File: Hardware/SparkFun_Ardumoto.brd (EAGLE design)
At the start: 59.7 x 53.3 mm, 33 parts, among them U1 ARDUINO, U2 L298, U3 74HC1G04, U4 74HC1G04

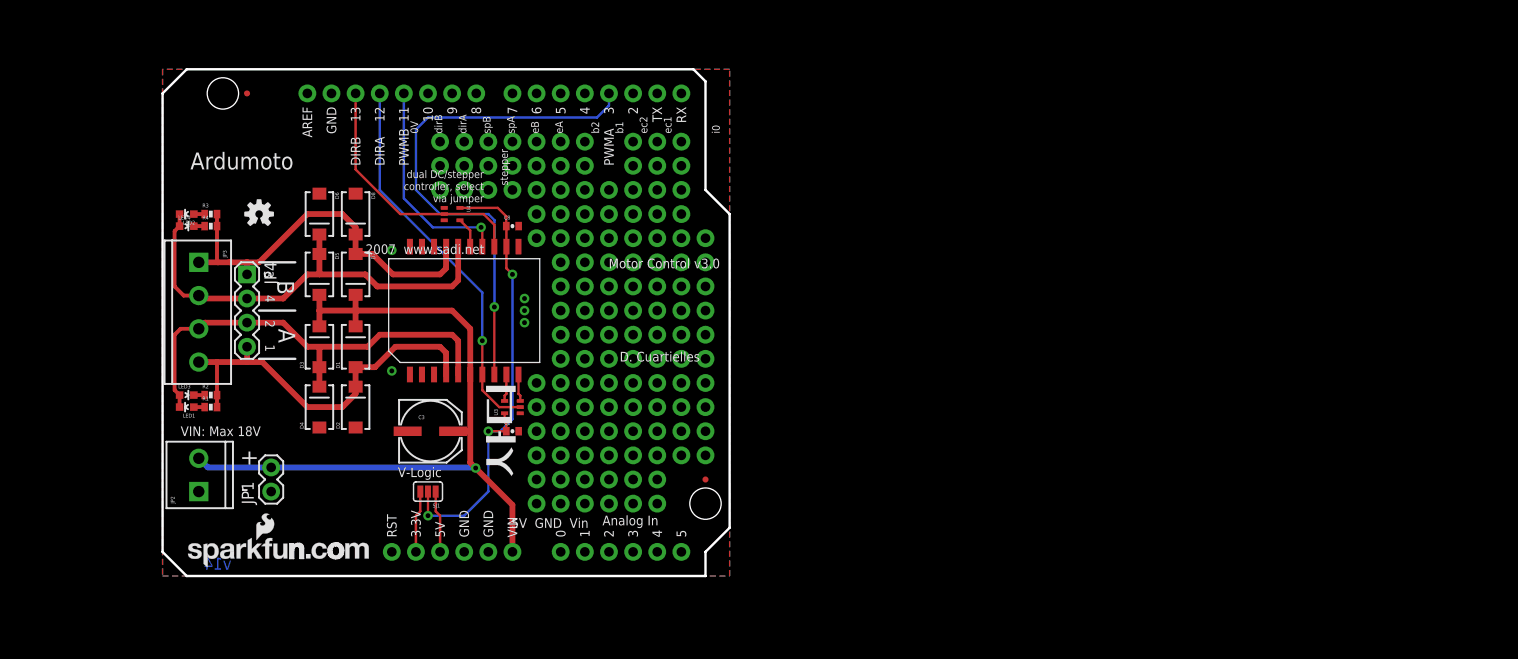
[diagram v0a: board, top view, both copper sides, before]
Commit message: Schematic is the same, but all parts have been updated to the new libraries.  The layout is no longer valid, and proto area has been moved aside.  This is ready for functional changes.
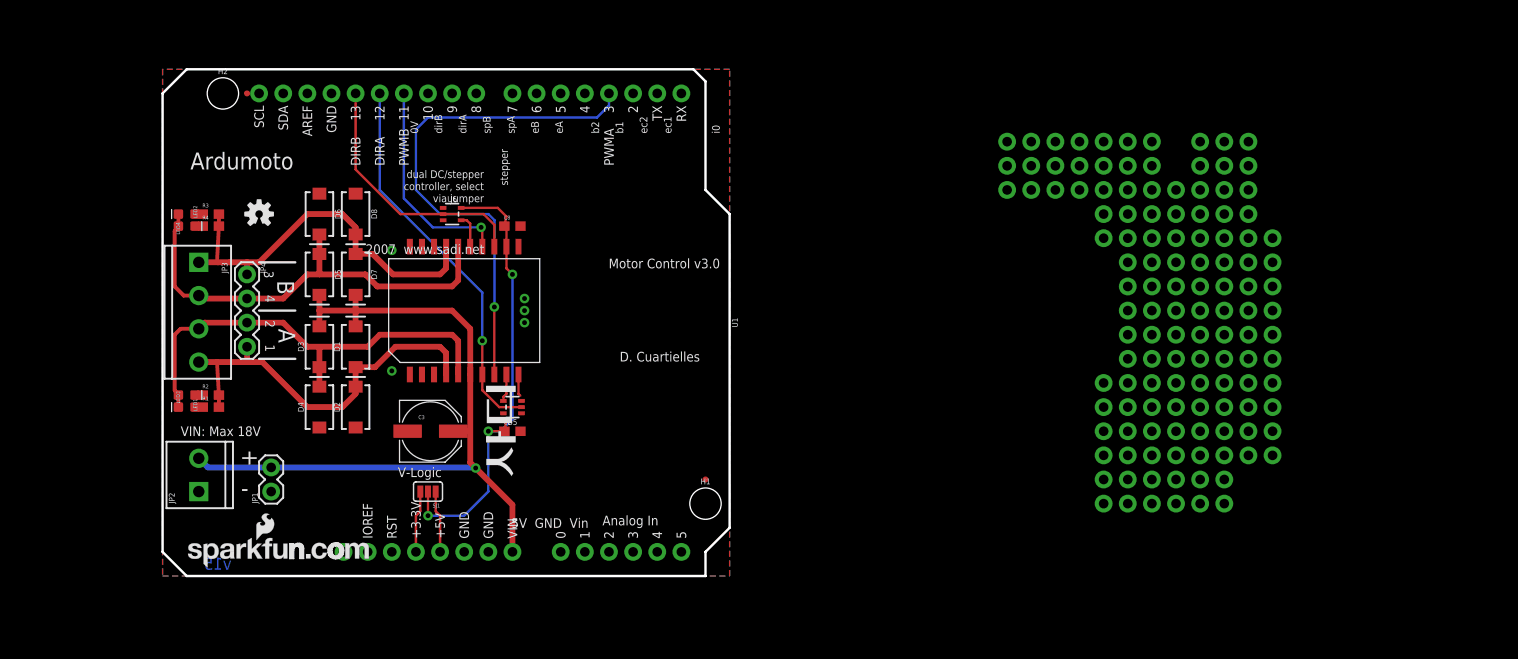
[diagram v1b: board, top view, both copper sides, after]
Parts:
- removed U3, U4: 74HC1G04, SparkFun:SC70
- added H1, H2: STAND-OFF, SparkFun-Hardware:STAND-OFF
- added U5, U6: 74HC1G04, SparkFun-IC-Logic:SOT353
- C1, C8: device SparkFun:0402-CAP -> SparkFun-Capacitors:0603
- C3: value 100uF,25V -> 100uF; device SparkFun:NIPPON_F80 -> SparkFun-Capacitors:PANASONIC_D
- D1, D2, D3, D4, D5, D6, D7, D8: value MBRA140 -> 1A/40V/500mV; device SparkFun:SMA-DIODE -> SparkFun-DiscreteSemi:SMA-DIODE
- JP1: device SparkFun:1X02 -> SparkFun-Connectors:1X02
- JP2: device SparkFun:SCREWTERMINAL-3.5MM-2 -> SparkFun-Connectors:SCREWTERMINAL-3.5MM-2
- JP3: device SparkFun:SCREWTERMINAL-3.5MM-4 -> SparkFun-Connectors:SCREWTERMINAL-3.5MM-4
- JP4: device SparkFun:1X04 -> SparkFun-Connectors:1X04
- LED1, LED2: device SparkFun:LED-0603 -> SparkFun-LED:LED-0603
- LED3, LED4: value Blue -> BLUE; device SparkFun:LED-0603 -> SparkFun-LED:LED-0603
- R1, R2, R3, R4: value 1K -> 1k; device SparkFun:0402-RES -> SparkFun-Resistors:0603
- U1: device SparkFun:DUEMILANOVE_SHIELD_NOLABELS -> SparkFun-Boards:UNO_R3_SHIELD
- U2: value L298 -> L298P013; device SparkFun:POWERSO20 -> SparkFun-IC-Special-Function:POWERSO20
- moved U1 39.6 mm to (29.2, 26.7)
- turned LED1 to 180 degrees
- turned LED2 to 180 degrees
- turned LED3 to 0 degrees
- turned LED4 to 0 degrees
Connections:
- net DIRA: now also U5.2; no longer U3.2
- net DIRB: now also U6.2; no longer U4.2
- net GND: now also U6.3; no longer U3.3, U4.3
- net N$1: now also U5.4; no longer U3.4
- net N$2: now also U6.4; no longer U4.4
- net V-LOGIC: now also U6.5; no longer U3.5, U4.5
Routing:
- net V-LOGIC: track 50.1 -> 49.4 mm
- net GND: track 2.88 -> 2.30 mm
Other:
- board text added: "v15"
- board text removed: "0"
- board text removed: "10"
- board text removed: "11"
- board text removed: "12"
- board text removed: "13"
- board text removed: "3.3V"
- board text removed: "5"
- board text removed: "5V"
- board text removed: "6"
- board text removed: "7"
- board text removed: "8"
- board text removed: "9"
- board text removed: "AREF"
- board text removed: "GND"
- board text removed: "RST"
- board text removed: "RX"
- board text removed: "TX"
- board text removed: "VIN"
- board text removed: "v14"

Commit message: Schematic changes applied, layout is now mostly ripped up
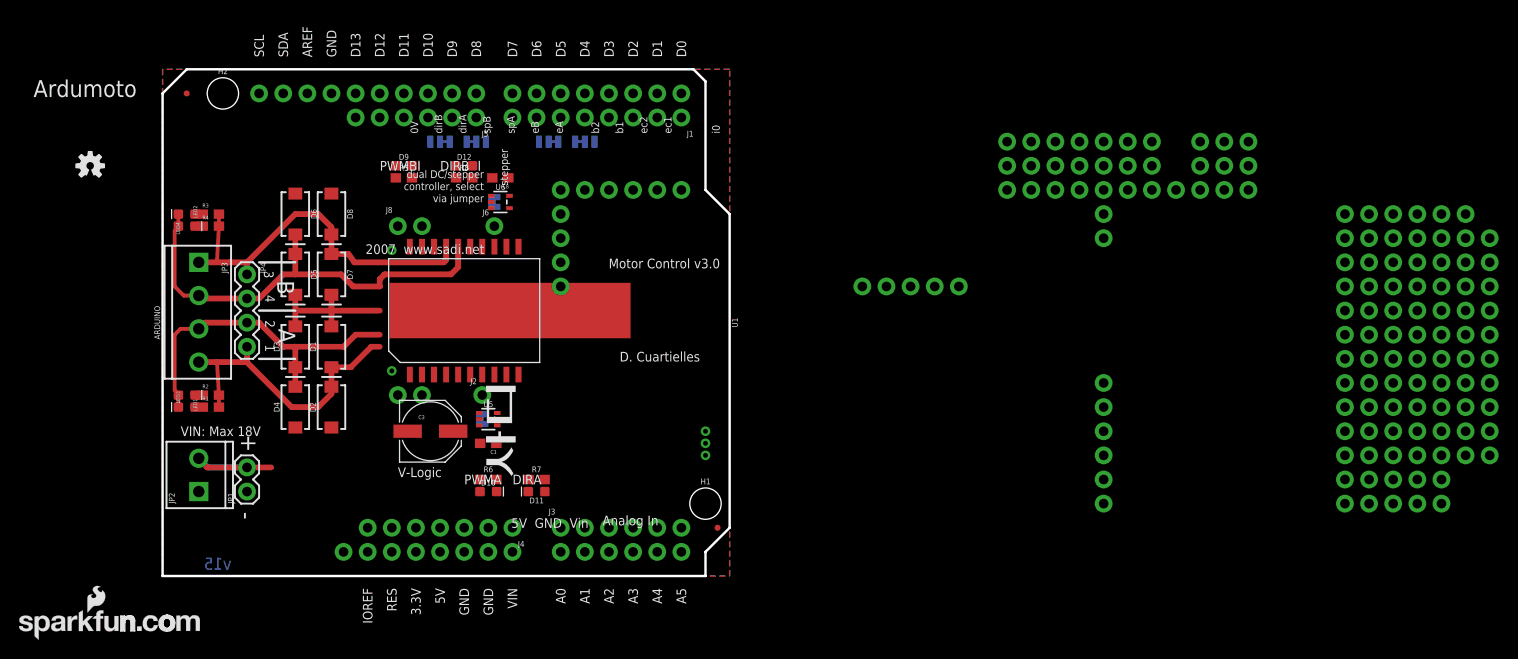
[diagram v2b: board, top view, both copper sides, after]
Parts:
- removed SJ1: (no value), SparkFun:SJ_3_PASTE1&2
- added D10, D11, D12, D9: RED, SparkFun-LED:LED-0603
- added J1: (no value), SparkFun-Connectors:1X08_NO_SILK
- added J2, J6: (no value), SparkFun-Connectors:1X01_NO_SILK
- added J3, J5: (no value), SparkFun-Connectors:1X06_NO_SILK
- added J4: (no value), SparkFun-Connectors:1X07_NO_SILK
- added J7, J8: (no value), SparkFun-Connectors:1X02_NO_SILK
- added JP10, JP7, JP8, JP9: JUMPER-SMT_3_1-NC_TRACE_SILK, SparkFun-Jumpers:SMT-JUMPER_3_1-NC_TRACE_SILK
- added JP11, JP12: JUMPER-SMT_2_NC_TRACE_SILK, SparkFun-Jumpers:SMT-JUMPER_2_NC_TRACE_SILK
- added R5, R6, R7, R8: 1k, SparkFun-Resistors:0603
- U1: device SparkFun-Boards:UNO_R3_SHIELD -> SparkFun-Boards:UNO_R3_SHIELD_NOLABELS
- moved U$10 19.3 mm to (-15.1, -6.73)
- moved U$1 18.5 mm to (-7.62, 43.2)
- moved JP5 6.35 mm to (2.54, 50.8)
- moved U6 5.24 mm to (35.6, 39.4)
- moved JP6 5.24 mm to (58.4, 5.08)
- moved C8 5.24 mm to (35.6, 41.9), turned to 180 degrees
- moved C1 2.84 mm to (34.3, 14.0), turned to 180 degrees
- moved U5 2.84 mm to (34.3, 16.5), turned to 270 degrees
- moved D3 2.54 mm to (14.0, 24.1)
- moved D4 2.54 mm to (14.0, 17.8)
- moved D5 2.54 mm to (14.0, 31.8)
- moved D6 2.54 mm to (14.0, 38.1)
- moved D1 2.54 mm to (17.8, 24.1)
- moved D2 2.54 mm to (17.8, 17.8)
- moved D7 2.54 mm to (17.8, 31.8)
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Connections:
- net N$1 renamed IN2
- net N$2 renamed IN4
- removed net V-LOGIC: C1.1, C8.1, SJ1.2, U2.12, U6.5
- new net D0: J1.1, U1.RX
- new net D1: J1.2, U1.TX
- new net D10: J5.3, JP10.1, U1.D10
- new net D11: J5.4, U1.D11
- new net D12: J5.5, U1.D12
- new net D13: J5.6, U1.D13
- new net D2: J1.3, JP7.1, U1.D2
- new net D3: J1.4, JP8.1, U1.D3
- new net D4: J1.5, U1.D4
- new net D5: J1.6, JP9.3, U1.D5
- new net D6: J1.7, JP9.1, U1.D6
- new net D7: J1.8, JP7.3, U1.D7
- new net D8: J5.1, JP8.3, U1.D8
- new net D9: J5.2, JP10.3, U1.D9
- new net IN1: J2.1, JP11.2, U2.7
- new net IN3: J6.1, JP12.1, U2.13
- new net IOREF: J4.7, U1.IOREF
- new net N$11: J8.2, U2.19
- new net N$14: J7.1, U2.2
- new net N$21: J3.1, U1.A0
- new net N$22: J3.2, U1.A1
- new net N$23: J3.3, U1.A2
- new net N$24: J3.4, U1.A3
- new net N$25: J3.5, U1.A4
- new net N$26: J3.6, U1.A5
- new net N$36: D9.A, R5.1
- new net N$37: D10.A, R6.1
- new net N$38: D12.A, R8.1
- new net N$39: D11.A, R7.1
- new net RESET: J4.6, U1.RES
- net 3.3V: now also J4.5; no longer SJ1.3
- net 5V: now also C1.1, C8.1, J4.4, U2.12, U5.5, U6.5; no longer SJ1.1
- net DIRA: now also JP11.1, JP8.2, R7.2; no longer U1.D12, U2.7
- net DIRB: now also JP12.2, JP7.2, R8.2; no longer U1.D13, U2.13
- net GND: now also D10.C, D11.C, D12.C, D9.C, J4.2, J4.3, J7.2, J8.1, U5.3; no longer U2.19, U2.2
- net PWMA: now also JP9.2, R6.2; no longer U1.D3
- net PWMB: now also JP10.2, R5.2; no longer U1.D11
- net VIN: now also J4.1
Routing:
- net PWMA: track 54.8 -> 0.00 mm, vias 1 -> 0
- net VIN: track 80.0 -> 29.0 mm, vias 1 -> 0
- net V-LOGIC: track 49.4 -> 0.00 mm, vias 3 -> 0
- net DIRA: track 40.6 -> 0.00 mm, vias 1 -> 0
- net DIRB: track 27.3 -> 0.00 mm
- net PWMB: track 22.5 -> 0.00 mm, vias 1 -> 0
- net OUT2: track 47.7 -> 35.6 mm
- net OUT1: track 41.2 -> 31.7 mm
- net 5V: track 6.54 -> 0.00 mm
- net 3.3V: track 6.54 -> 0.00 mm
- net IN4: track 3.52 -> 0.00 mm
- net IN2: track 2.91 -> 0.00 mm
- net GND: track 2.30 -> 0.00 mm
- net OUT3: track 41.5 -> 40.0 mm
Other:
- outline, holes or cut-outs redrawn
- board text added: "3.3V"
- board text added: "5V"
- board text added: "A0"
- board text added: "A1"
- board text added: "A2"
- board text added: "A3"
- board text added: "A4"
- board text added: "A5"
- board text added: "AREF"
- board text added: "D0"
- board text added: "D1"
- board text added: "D10"
- board text added: "D11"
- board text added: "D12"
- board text added: "D13"
- board text added: "D2"
- board text added: "D3"
- board text added: "D4"
- board text added: "D5"
- board text added: "D6"
- board text added: "D7"
- board text added: "D8"
- board text added: "D9"
- board text added: "GND"
- board text added: "IOREF"
- board text added: "RES"
- board text added: "SCL"
- board text added: "SDA"
- board text added: "VIN"

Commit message: Desing ready for proto 1 review
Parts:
- removed JP11, JP12: JUMPER-SMT_2_NC_TRACE_SILK, SparkFun-Jumpers:SMT-JUMPER_2_NC_TRACE_SILK
- removed U$10: LOGO-SFENEW, SparkFun:SFE-NEW-WEBLOGO
- removed U$11: CREATIVE_COMMONS, SparkFun:CREATIVE_COMMONS
- added FD1, FD2: FIDUCIALUFIDUCIAL, SparkFun:MICRO-FIDUCIAL
- added FRAME1: FRAME-LETTER, SparkFun-Aesthetics:CREATIVE_COMMONS
- added FRAME2: FRAME-LETTERNO_PACKAGE, SparkFun-Aesthetics:DUMMY
- added J10: (no value), SparkFun-Connectors:SCREWTERMINAL-3.5MM-2
- added J11, J12, J13, J14: (no value), SparkFun-Connectors:1X01_NO_SILK
- added J9: (no value), SparkFun-Connectors:1X02
- added LOGO1: SFE_LOGO_NAME_FLAME.2_INCH, SparkFun-Aesthetics:SFE_LOGO_NAME_FLAME_.2
- added LOGO2: SFE_LOGO_NAME.1_INCH, SparkFun-Aesthetics:SFE_LOGO_NAME_.1
- J7: device SparkFun-Connectors:1X02_NO_SILK -> SparkFun-Connectors:SCREWTERMINAL-3.5MM-4
- J8: device SparkFun-Connectors:1X02_NO_SILK -> SparkFun-Connectors:1X04
- JP1: value (none) -> 31NCT; device SparkFun-Connectors:1X02 -> SparkFun-Jumpers:SMT-JUMPER_3_1-NC_TRACE_SILK
- JP10, JP9: value JUMPER-SMT_3_1-NC_TRACE_SILK -> (none); device SparkFun-Jumpers:SMT-JUMPER_3_1-NC_TRACE_SILK -> SparkFun-Connectors:1X02_NO_SILK
- JP2: value (none) -> 31NCT; device SparkFun-Connectors:SCREWTERMINAL-3.5MM-2 -> SparkFun-Jumpers:SMT-JUMPER_3_1-NC_TRACE_SILK
- JP3: value (none) -> 31NCT; device SparkFun-Connectors:SCREWTERMINAL-3.5MM-4 -> SparkFun-Jumpers:SMT-JUMPER_3_1-NC_TRACE_SILK
- JP4: value (none) -> 31NCT; device SparkFun-Connectors:1X04 -> SparkFun-Jumpers:SMT-JUMPER_3_1-NC_TRACE_SILK
- JP5, JP6: value FIDUCIALUFIDUCIAL -> 2NCT; device SparkFun:MICRO-FIDUCIAL -> SparkFun-Jumpers:SMT-JUMPER_2_NC_TRACE_SILK
- JP7, JP8: value JUMPER-SMT_3_1-NC_TRACE_SILK -> 2NCT; device SparkFun-Jumpers:SMT-JUMPER_3_1-NC_TRACE_SILK -> SparkFun-Jumpers:SMT-JUMPER_2_NC_TRACE_SILK
- U2: value L298P013 -> L298; device SparkFun-IC-Special-Function:POWERSO20 -> SparkFun-IC-Special-Function:POWERSO20_L298_PAD
- moved JP1 53.0 mm to (47.0, 45.7), flipped to the bottom, turned to 0 degrees
- moved JP2 52.1 mm to (40.6, 45.7), flipped to the bottom, turned to 180 degrees
- moved JP5 44.6 mm to (31.1, 16.5), flipped to the bottom, turned to 90 degrees
- moved JP9 33.6 mm to (24.1, 16.5), turned to 0 degrees
- moved JP3 33.0 mm to (34.3, 45.7), flipped to the bottom, turned to 0 degrees
- moved D11 32.4 mm to (7.62, 2.41)
- moved R7 29.0 mm to (11.4, 2.41)
- moved JP6 27.3 mm to (33.7, 16.5), flipped to the bottom, turned to 90 degrees
- moved D10 27.1 mm to (7.62, 3.81), turned to 180 degrees
- moved J7 26.8 mm to (3.81, 31.9), flipped to the top, turned to 270 degrees
- moved U$1 24.4 mm to (16.5, 47.0)
- moved D12 24.1 mm to (7.62, 43.1), turned to 180 degrees
- moved R6 23.7 mm to (11.4, 3.81)
- moved JP4 23.6 mm to (27.9, 45.7), flipped to the bottom, turned to 180 degrees
- moved R8 20.4 mm to (11.4, 43.1)
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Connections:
- new net NDIRA: JP6.1, U5.4
- new net NDIRB: JP7.2, U6.4
- net D10: now also JP4.1; no longer JP10.1
- net D2: now also JP3.1; no longer JP7.1
- net D3: now also JP1.1; no longer JP8.1
- net D5: now also JP2.3; no longer JP9.3
- net D6: now also JP2.1; no longer JP9.1
- net D7: now also JP3.3; no longer JP7.3
- net D8: now also JP1.3; no longer JP8.3
- net D9: now also JP4.3; no longer JP10.3
- net DIRA: now also JP1.2, JP5.1; no longer JP11.1, JP8.2
- net DIRB: now also JP3.2, JP8.2; no longer JP12.2, JP7.2
- net GND: now also J10.1, J9.1, JP10.1, JP9.2, U2.PAD; no longer J7.2, J8.1, JP1.1, JP2.1
- net IN1: now also JP5.2; no longer JP11.2
- net IN2: now also J14.1, JP6.2; no longer U5.4
- net IN3: now also JP8.1; no longer JP12.1
- net IN4: now also J13.1, JP7.1; no longer U6.4
- net N$11: now also JP10.2; no longer J8.2
- net N$14: now also JP9.1; no longer J7.1
- net N$8: now also LED4.C; no longer LED2.A
- net N$9: now also LED2.A; no longer LED4.C
- net OUT1: now also J7.4, J8.4; no longer JP3.4, JP4.4
- net OUT2: now also J7.3, J8.3; no longer JP3.3, JP4.3
- net OUT3: now also D5.A, D6.C, J7.2, J8.2, LED2.C, LED4.A, U2.16; no longer D7.A, D8.C, JP3.1, JP4.1, R3.2, R4.2, U2.17
- net OUT4: now also D7.A, D8.C, J7.1, J8.1, R3.2, R4.2, U2.17; no longer D5.A, D6.C, JP3.2, JP4.2, LED2.C, LED4.A, U2.16
- net PWMA: now also J11.1, JP2.2; no longer JP9.2
- net PWMB: now also J12.1, JP4.2; no longer JP10.2
- net VIN: now also J10.2, J9.2; no longer JP1.2, JP2.2
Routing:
- net DIRA: track 0.00 -> 95.0 mm, vias 0 -> 2
- net PWMA: track 0.00 -> 87.5 mm, vias 0 -> 2
- net VIN: track 29.0 -> 114.7 mm, vias 0 -> 3
- net 5V: track 0.00 -> 66.7 mm, vias 0 -> 3
- net PWMB: track 0.00 -> 42.8 mm, vias 0 -> 1
- net DIRB: track 0.00 -> 33.5 mm, vias 0 -> 1
- net D2: track 0.00 -> 20.2 mm, vias 0 -> 1
- net IN1: track 0.00 -> 17.5 mm, vias 0 -> 1
- net IN4: track 0.00 -> 17.0 mm, vias 0 -> 1
- net D8: track 0.00 -> 16.5 mm, vias 0 -> 1
- net OUT1: track 31.7 -> 44.8 mm
- net IN3: track 0.00 -> 11.9 mm, vias 0 -> 1
- net IN2: track 0.00 -> 10.6 mm, vias 0 -> 1
- net N$14: track 0.00 -> 8.77 mm
- net N$11: track 0.00 -> 8.77 mm
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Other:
- board text added: "10"
- board text added: "5"
- board text added: "6"
- board text added: "7"
- board text added: "8"
- board text added: "9"
- board text added: "DISCONNECTS"
- board text added: "DRIVE A"
- board text added: "DRIVE B"
- board text added: "IN1"
- board text added: "IN2"
- board text added: "IN3"
- board text added: "IN4"
- board text added: "IOR"
- board text added: "Max 18V"
- board text added: "PWM(EN)A"
- board text added: "PWM(EN)B"
- board text added: "Proto Area"
- board text added: "SELECT:"
- board text removed: "0V"
- board text removed: "2007 www.sadi.net"
- board text removed: "5V GND Vin"
- board text removed: "AREF"
- board text removed: "Analog In"
- board text removed: "D. Cuartielles"
- board text removed: "IOREF"
- board text removed: "Motor Control v3.0"
- board text removed: "SCL"
- board text removed: "SDA"
- board text removed: "V-Logic"
- board text removed: "VIN: Max 18V"
- board text removed: "b1"
- board text removed: "b2"
- board text removed: "controller, select"
- board text removed: "dirA"
- board text removed: "dirB"
- board text removed: "dual DC/stepper"
- board text removed: "eA"
- board text removed: "eB"
- board text removed: "ec1"
- board text removed: "ec2"
- board text removed: "i0"
- board text removed: "spA"
- board text removed: "spB"
- board text removed: "stepper"
- board text removed: "via jumper"
